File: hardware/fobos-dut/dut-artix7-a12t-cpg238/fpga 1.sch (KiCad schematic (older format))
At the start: 10 parts, among them U1 XC7A12T-CPG238, U9 IS25LP256D-JMLE

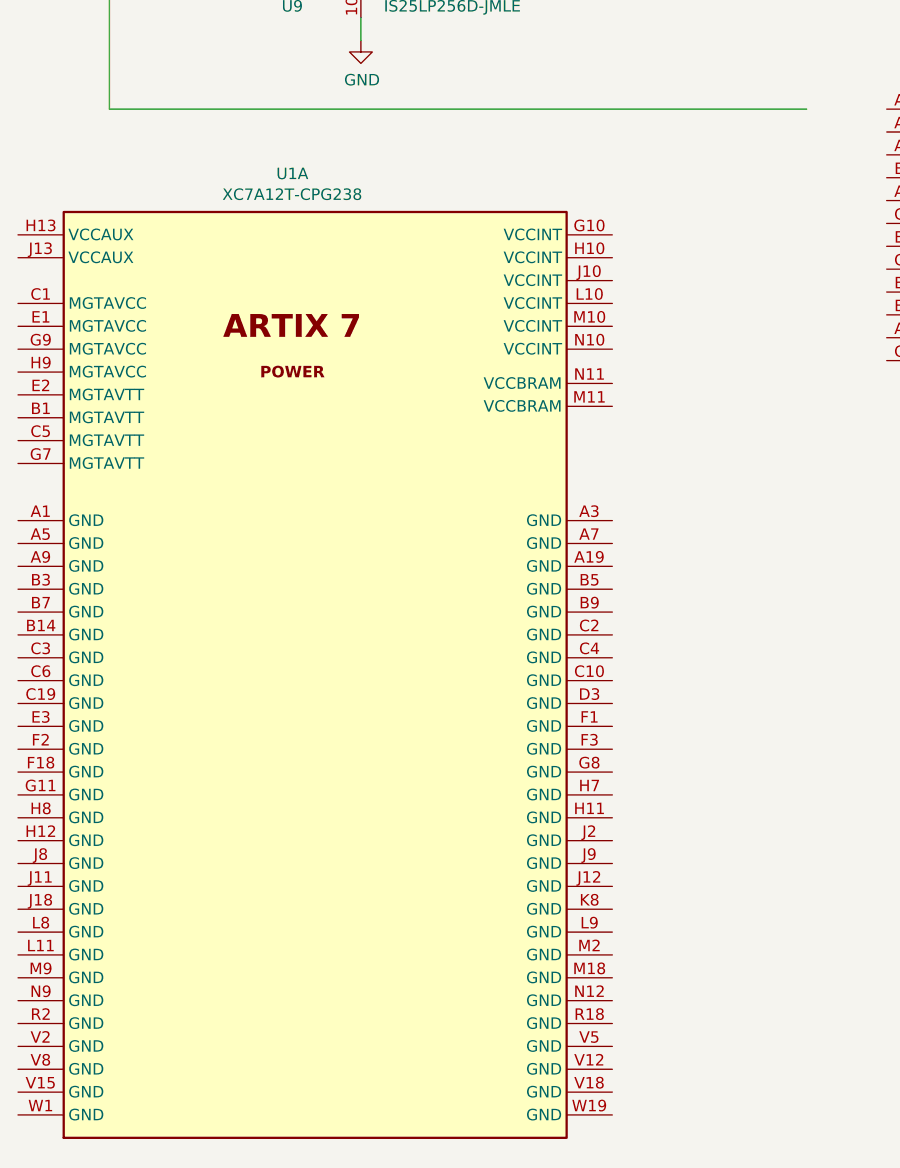
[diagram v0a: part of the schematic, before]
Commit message: Started to rewire the CPG238 into the schematic Split FPGA Power and Programming into two sheets since new FPGA symbol explicitly displays each power pin and is much larger
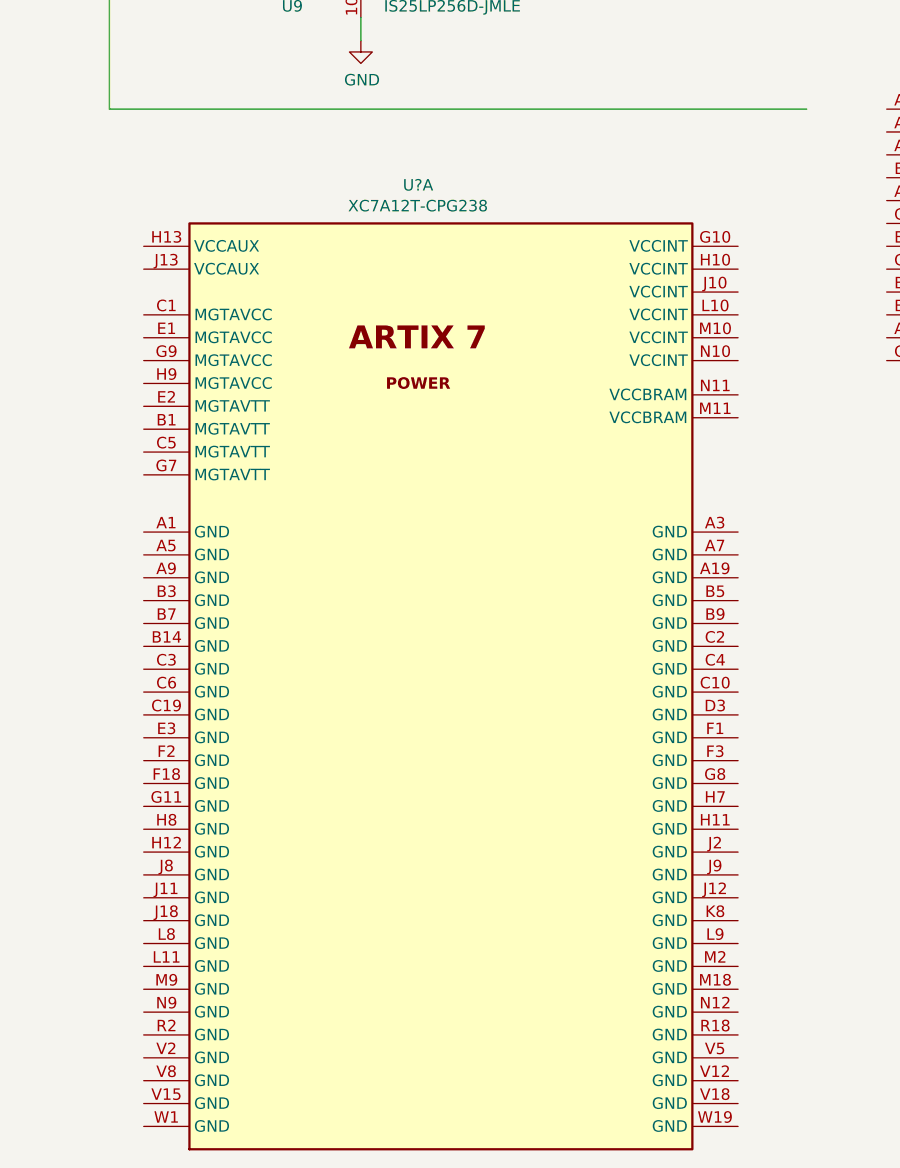
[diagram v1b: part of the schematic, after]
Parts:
- removed unit 1 of U1
- added U?: XC7A12T-CPG238, Package_BGA:Xilinx_CPG238, symbol cerg:XC7A12T-CPG238
- U1: footprint (none) -> Package_BGA:Xilinx_CPG238
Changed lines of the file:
@@
 $Descr USLetter 11000 8500
 encoding utf-8
-Sheet 4 7
+Sheet 4 8
 Title "FOBOS Artix-7 a12t DUT - FPGA "
 Date "2020-07-28"
@@
 $Comp
 L cerg:XC7A12T-CPG238 U1
-U 1 1 60B2ACB3
-P 850 4150
-F 0 "U1" H 2050 4417 50  0000 C CNN
-F 1 "XC7A12T-CPG238" H 2050 4326 50  0000 C CNN
-F 2 "" H 850 4150 50  0001 C CNN
-F 3 "" H 850 4150 50  0001 C CNN
-	1    850  4150
-	1    0    0    -1
-$EndComp
-$Comp
-L cerg:XC7A12T-CPG238 U1
 U 4 1 60B4EFD1
 P 4650 3600
 F 0 "U1" H 6880 3203 50  0000 L CNN
 F 1 "XC7A12T-CPG238" H 6880 3112 50  0000 L CNN
-F 2 "" H 4650 3600 50  0001 C CNN
+F 2 "Package_BGA:Xilinx_CPG238" H 4650 3600 50  0001 C CNN
 F 3 "" H 4650 3600 50  0001 C CNN
 	4    4650 3600
@@
 F 0 "U1" H 9780 4746 50  0000 L CNN
 F 1 "XC7A12T-CPG238" H 9780 4655 50  0000 L CNN
-F 2 "" H 7550 5300 50  0001 C CNN
+F 2 "Package_BGA:Xilinx_CPG238" H 7550 5300 50  0001 C CNN
 F 3 "" H 7550 5300 50  0001 C CNN
 	6    7550 5300
 	1    0    0    -1
 $EndComp
+$Comp
+L cerg:XC7A12T-CPG238 U?
+U 1 1 60D24ECB
+P 1400 4200
+F 0 "U?" H 2600 4467 50  0000 C CNN
+F 1 "XC7A12T-CPG238" H 2600 4376 50  0000 C CNN
+F 2 "Package_BGA:Xilinx_CPG238" H 1400 4200 50  0001 C CNN
+F 3 "" H 1400 4200 50  0001 C CNN
+	1    1400 4200
+	1    0    0    -1
+$EndComp

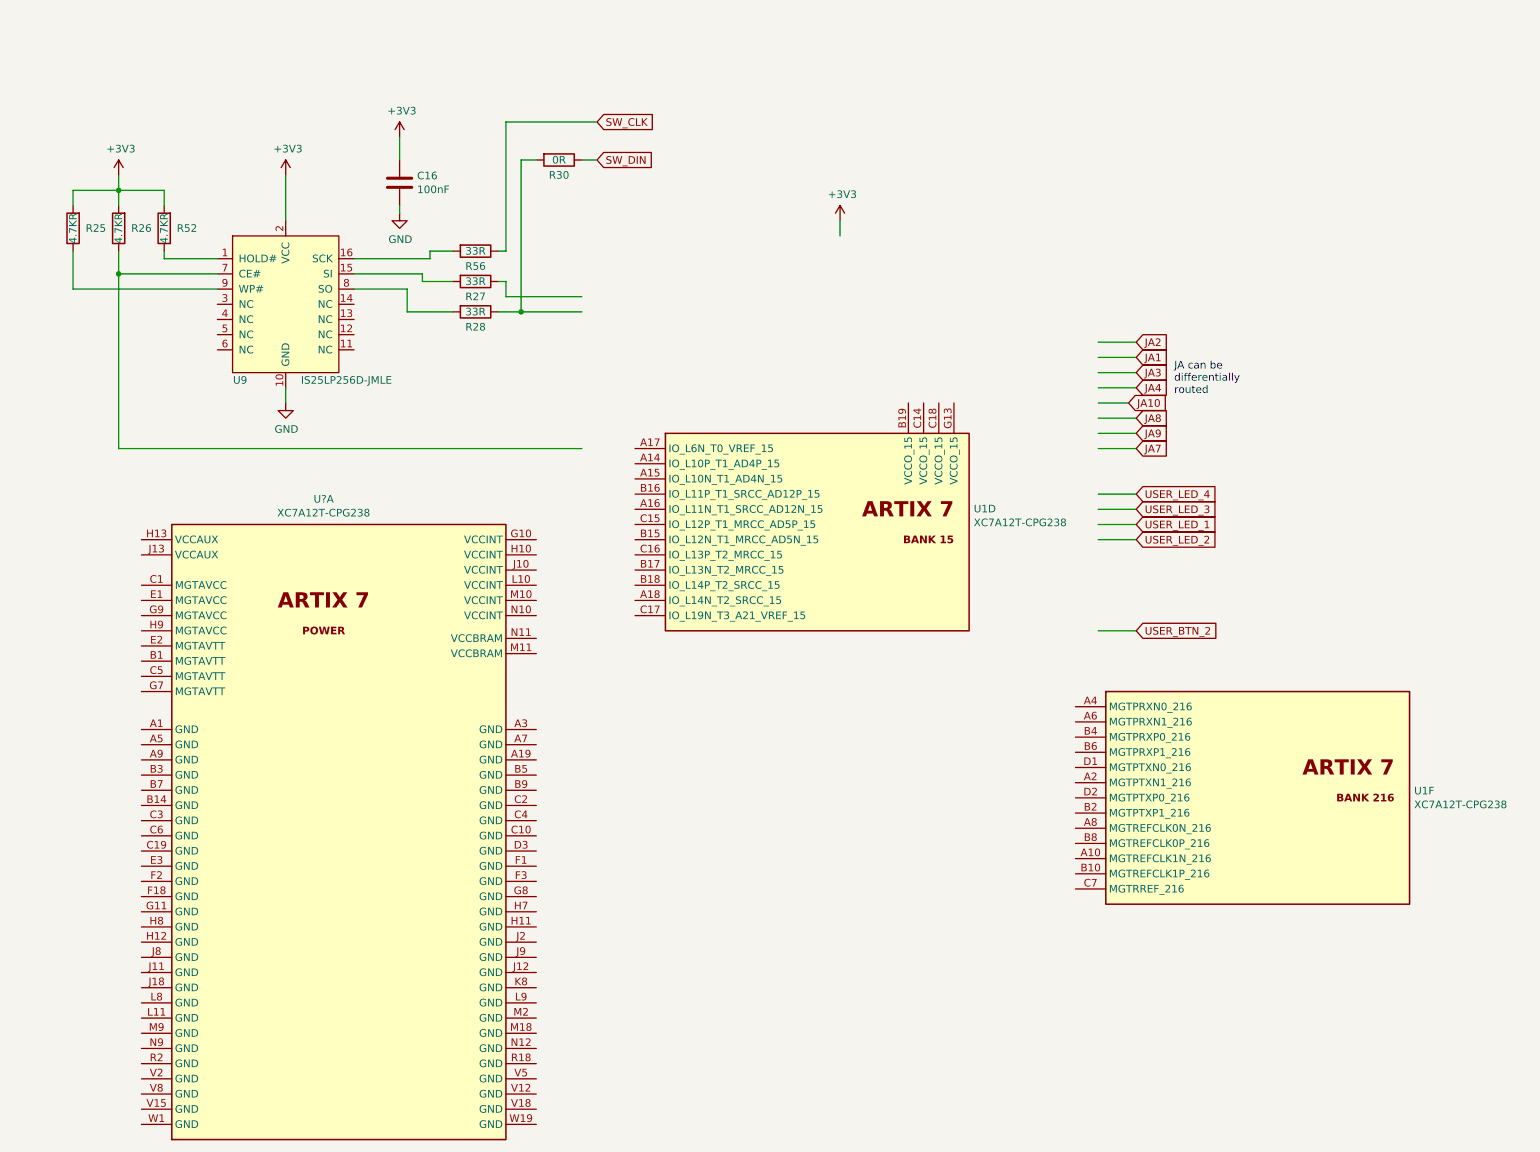
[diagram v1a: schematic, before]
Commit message: Connected the fixed signals to the FPGA, flexible IO are left unconnected Added 0.1 ohm resistors to the 1V8 and 3V3 power rails, added test points which allow for easy measurement Updated ARTIX7-A12T-CPG238 symbol to make schematic route similarly to the last symbol Connected CFGVBS signal to the 3V3 rail, was previously connected to VCCINT which was a mistake Ran through 7 Series schematic review checklist - 7_Series_Schematic_Review_Recommendations.xlsm Added Xilinx pinout files for the CPG238 package Generated schematic for the csg325 for easy referencing
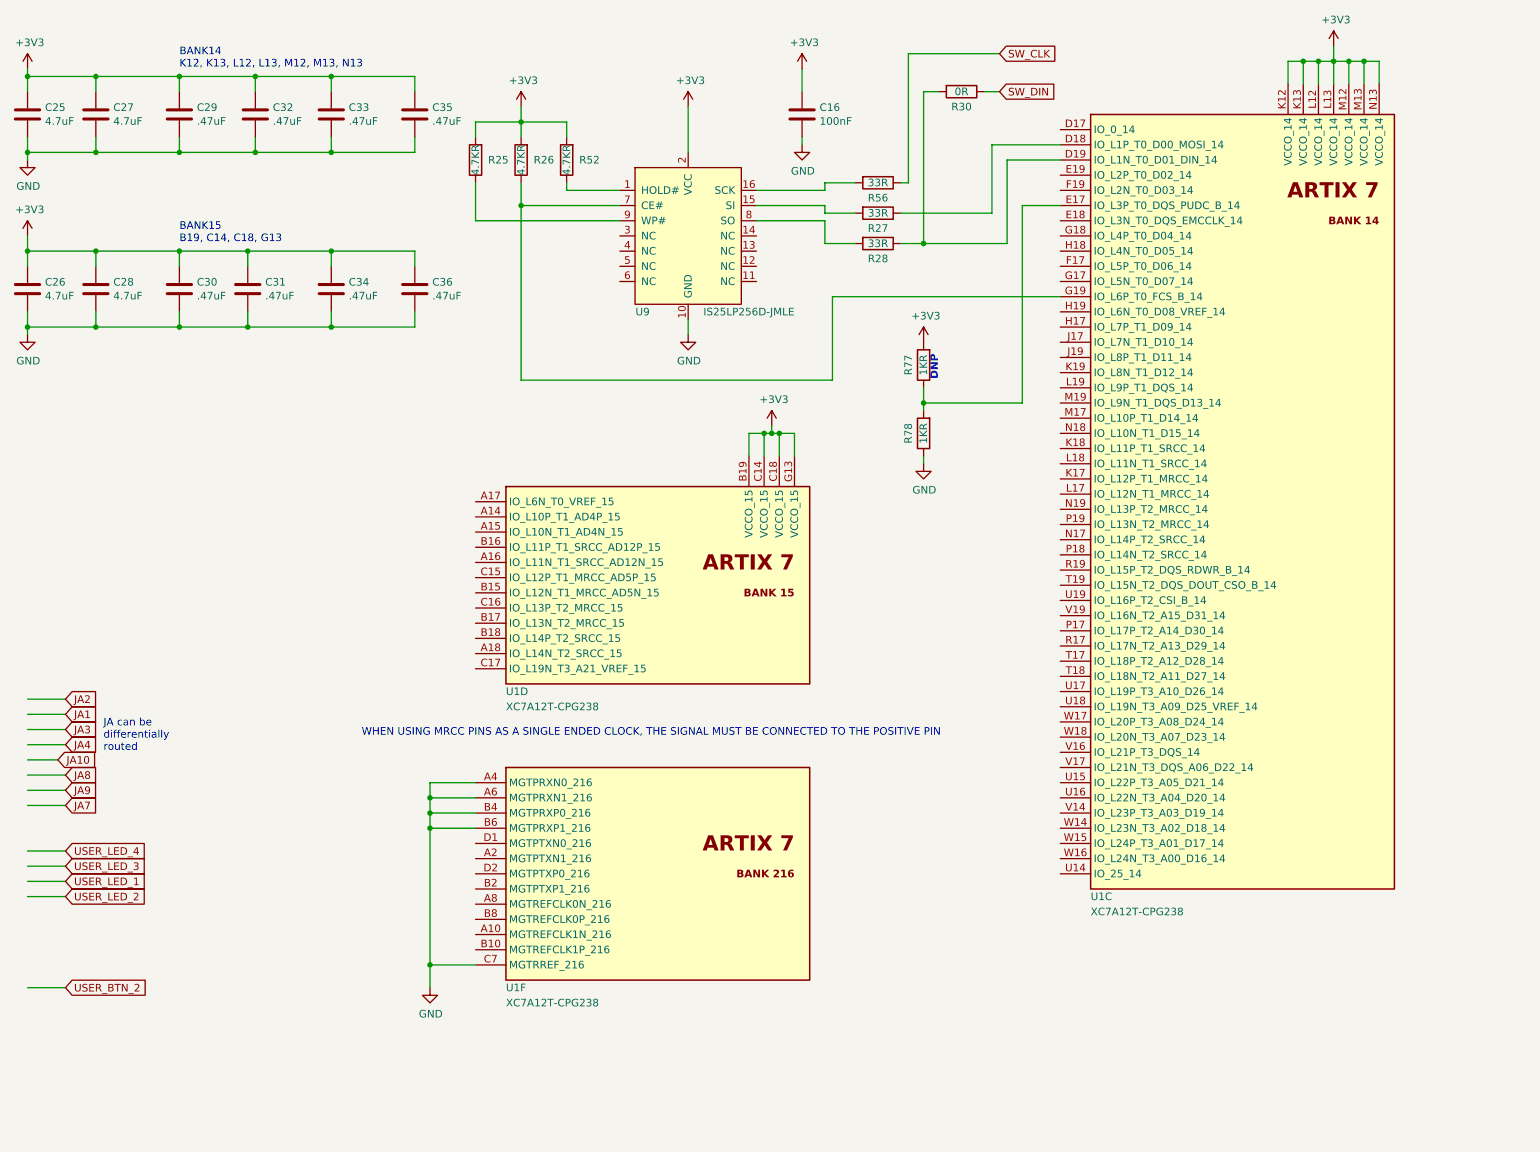
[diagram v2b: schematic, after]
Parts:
- removed U?: XC7A12T-CPG238, Package_BGA:Xilinx_CPG238, symbol cerg:XC7A12T-CPG238
- added C25, C26, C27, C28: 4.7uF, Capacitor_SMD:C_0402_1005Metric_Pad0.74x0.62mm_HandSolder, symbol Device:C
- added C29, C30, C31, C32, C33, C34, C35, C36: .47uF, Capacitor_SMD:C_0402_1005Metric_Pad0.74x0.62mm_HandSolder, symbol Device:C
- added R77, R78: 1KR, Resistor_SMD:R_0603_1608Metric, symbol Device:R
- added unit 3 of U1
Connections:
- wire segments 52 -> 142
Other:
- note added: "BANK14\nK12, K13, L12, L13, M12, M13, N13"
- note added: "BANK15\nB19, C14, C18, G13"
- note added: "DNP"
- note added: "WHEN USING MRCC PINS AS A SINGLE ENDED CLOCK, THE SIGNAL MUST BE CONNECTED TO THE POSITIVE PIN"
- moved on the sheet: C16, R25, R26, R27, R28, R30, R52, R56, U1D, U1F, U9

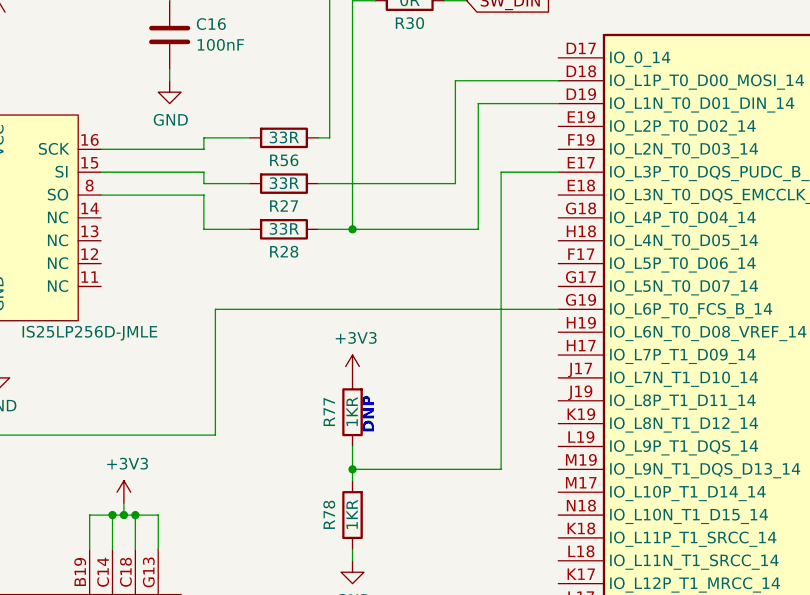
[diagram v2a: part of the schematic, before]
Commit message: updated library ref for diode and FET, placed target connector and some parts
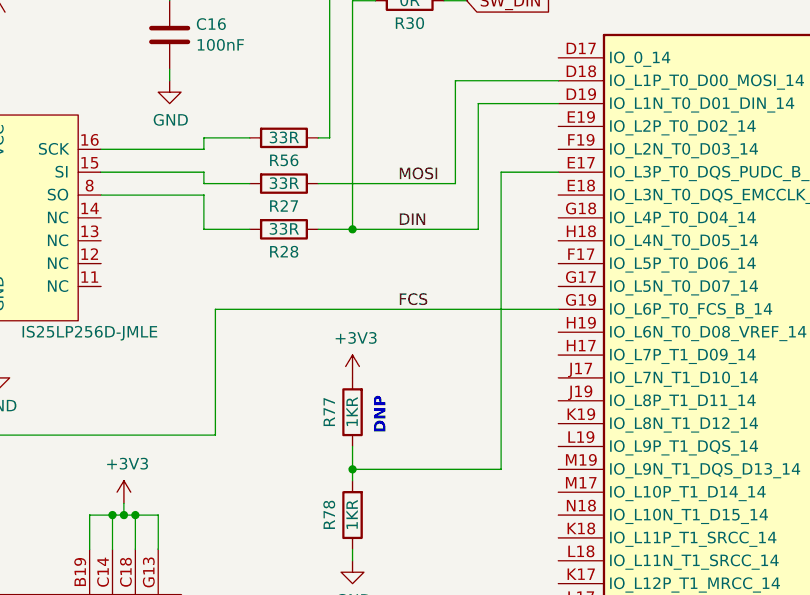
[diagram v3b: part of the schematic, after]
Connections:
- net labels added: DIN, FCS, MOSI
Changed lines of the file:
@@
 Wire Wire Line
 	7200 2000 7200 3300
-Text Notes 6650 3150 1    50   ~ 10
+Text Notes 6700 3150 1    50   ~ 10
 DNP
 $Comp
@@
 Text Notes 2850 5500 0    50   ~ 0
 WHEN USING MRCC PINS AS A SINGLE ENDED CLOCK, THE SIGNAL MUST BE CONNECTED TO THE POSITIVE PIN
+Text Label 6750 2050 0    50   ~ 0
+MOSI
+Text Label 6750 2250 0    50   ~ 0
+DIN
+Text Label 6750 2600 0    50   ~ 0
+FCS
 $EndSCHEMATC

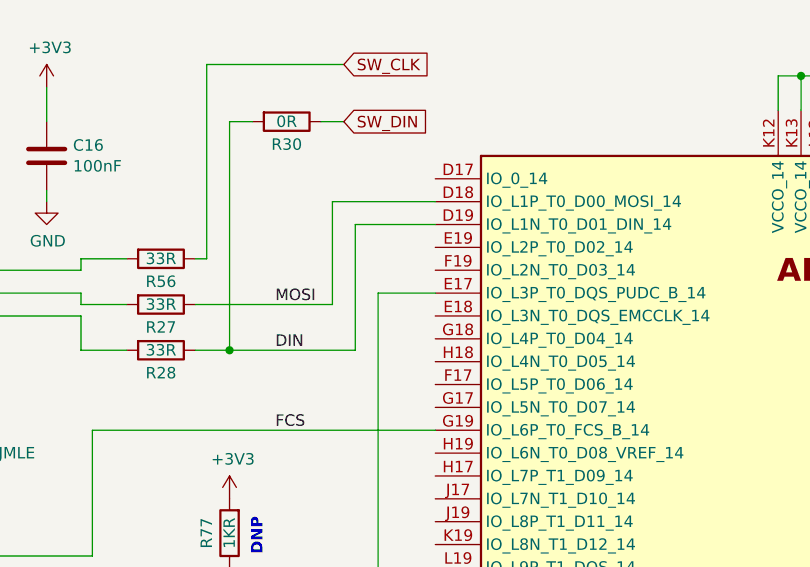
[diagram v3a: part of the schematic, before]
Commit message: few layout alignments incl space around FPGA
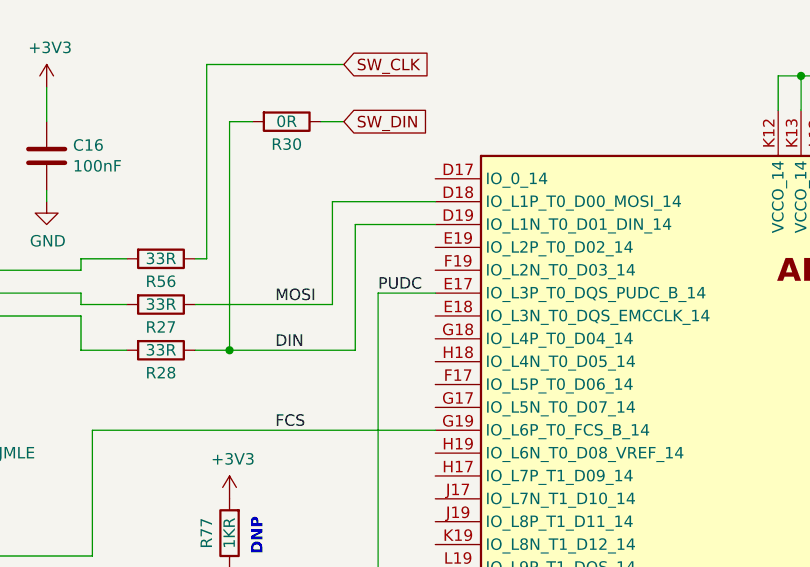
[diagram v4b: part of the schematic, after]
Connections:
- net labels added: PUDC
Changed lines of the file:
@@
 Text Label 6750 2600 0    50   ~ 0
 FCS
+Text Label 7200 2000 0    50   ~ 0
+PUDC
 $EndSCHEMATC
